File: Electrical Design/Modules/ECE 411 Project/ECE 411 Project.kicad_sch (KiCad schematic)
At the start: 31 parts, among them J1 5mm 9V Barrel, J2 BOOST, J3 Pheonix Connector, SW1 SW_Push, SW2 SW_Push, SW3 SW_Push, SW4 SW_Push, SW5 SW_Push, SW6 SW_Push, SW7 SW_Push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

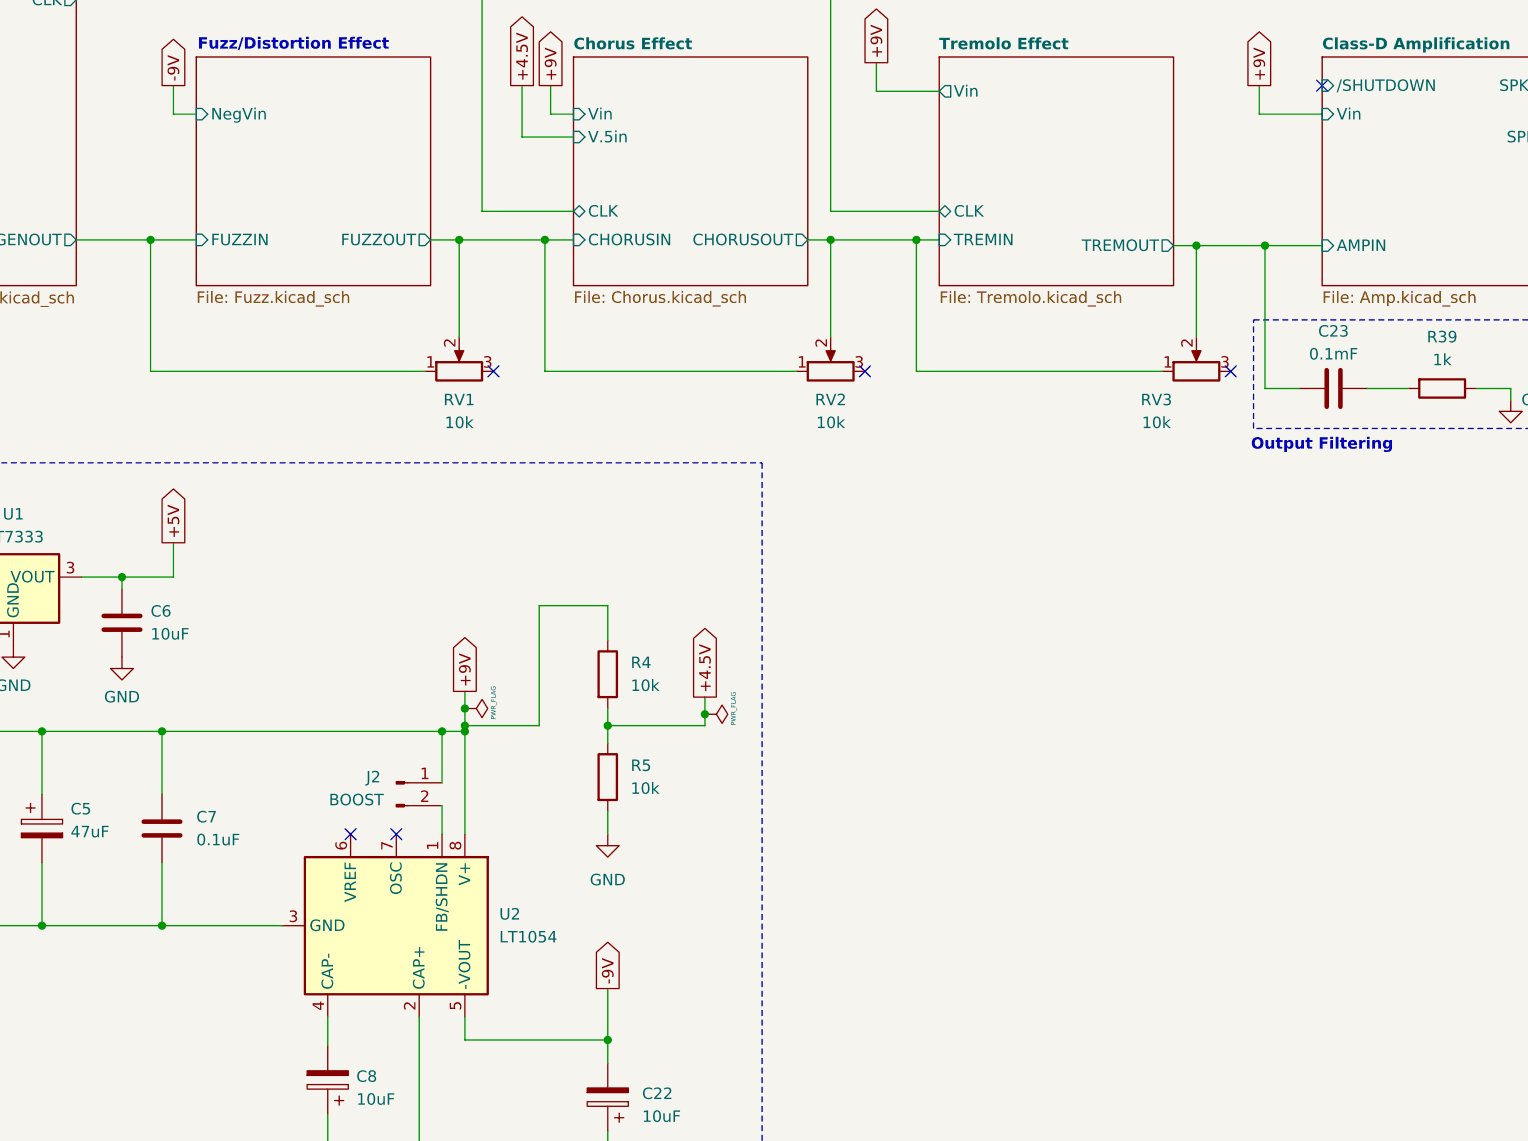
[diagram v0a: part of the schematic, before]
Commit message: bom changes
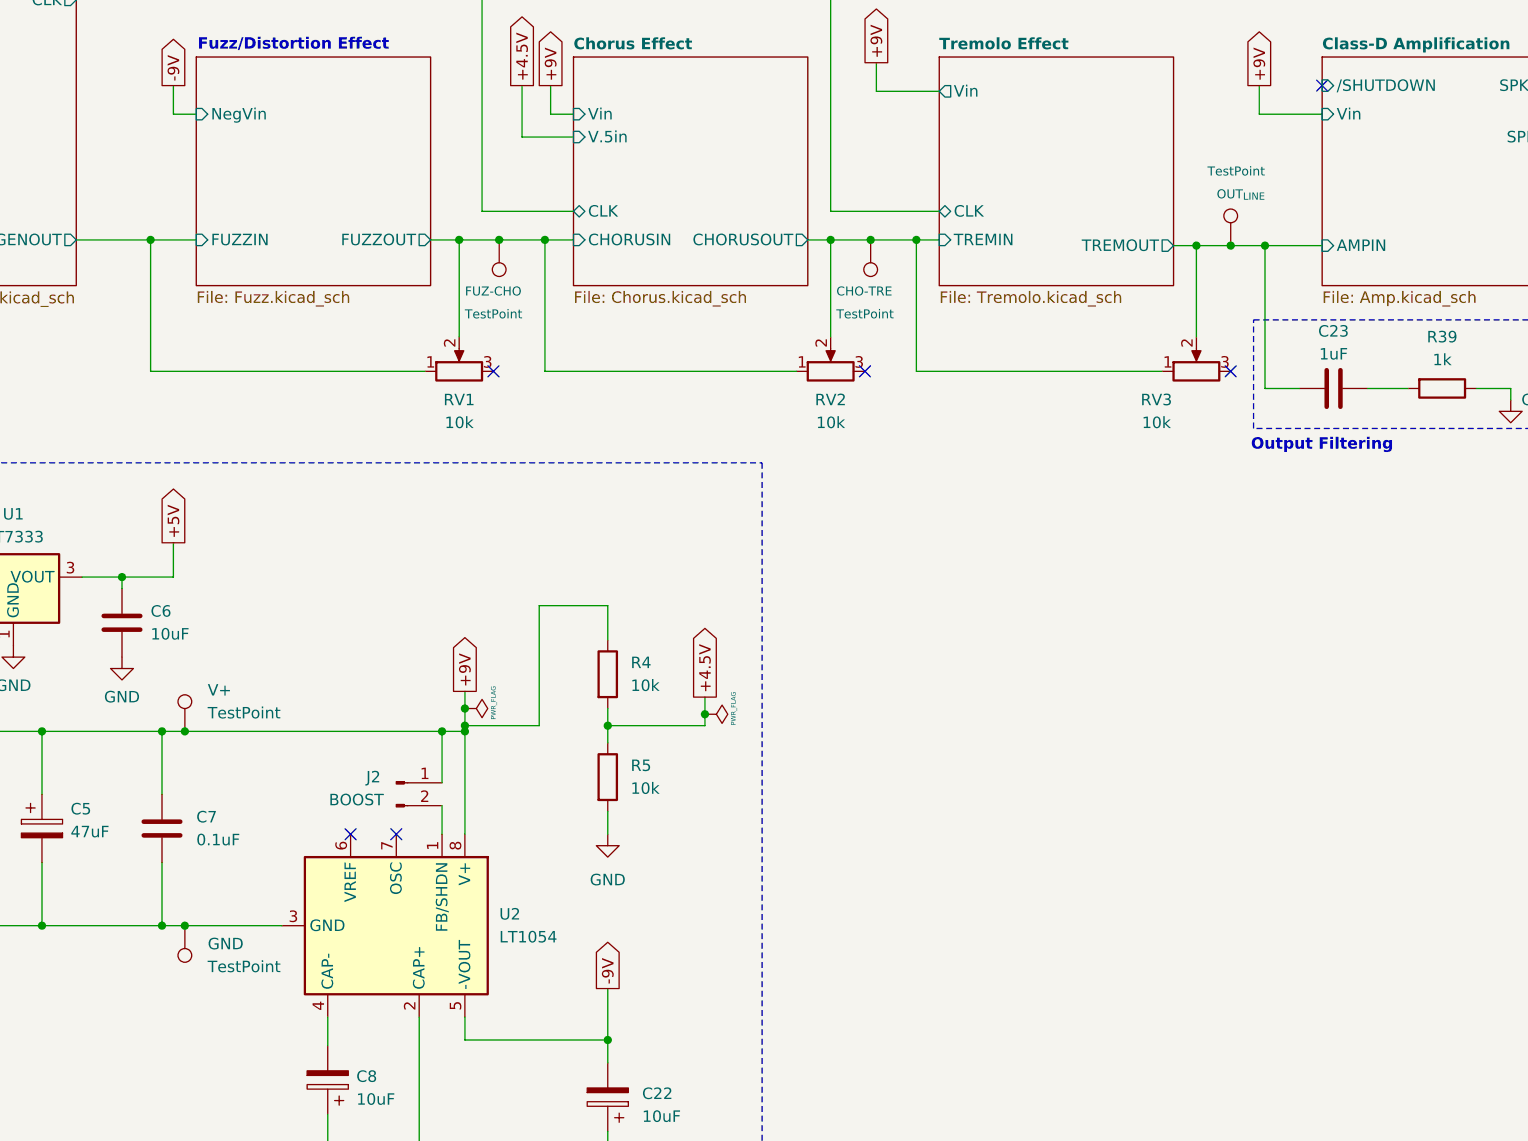
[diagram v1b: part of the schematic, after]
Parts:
- added CHO-TRE, FUZ-CHO, GND, OUT_{LINE}, V+: TestPoint, symbol Connector:TestPoint
- C22: On Hand (On Way) (none) -> (50); Part Number (none) -> UVR2C100MPD
- C23: value 0.1mF -> 1uF
- C43: On Hand (On Way) (none) -> (100); Part Number (none) -> CL21B104KBCNNNC
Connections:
- net +9V: now also V+.1
- net Chorus Effect/CHORUSIN: now also FUZ-CHO.1
- net Chorus Effect/CHORUSOUT: now also CHO-TRE.1
- net Class-D Amplification/AMPIN: now also OUT_{LINE}.1
- net GND: now also GND.1

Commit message: update kicad
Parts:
- OLED1: value ~ -> OLED-I2C
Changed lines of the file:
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@@
 			)
 		)
-		(property "Value" "~"
+		(property "Value" "OLED-I2C"
 			(at 94.615 45.72 0)
 			(effects

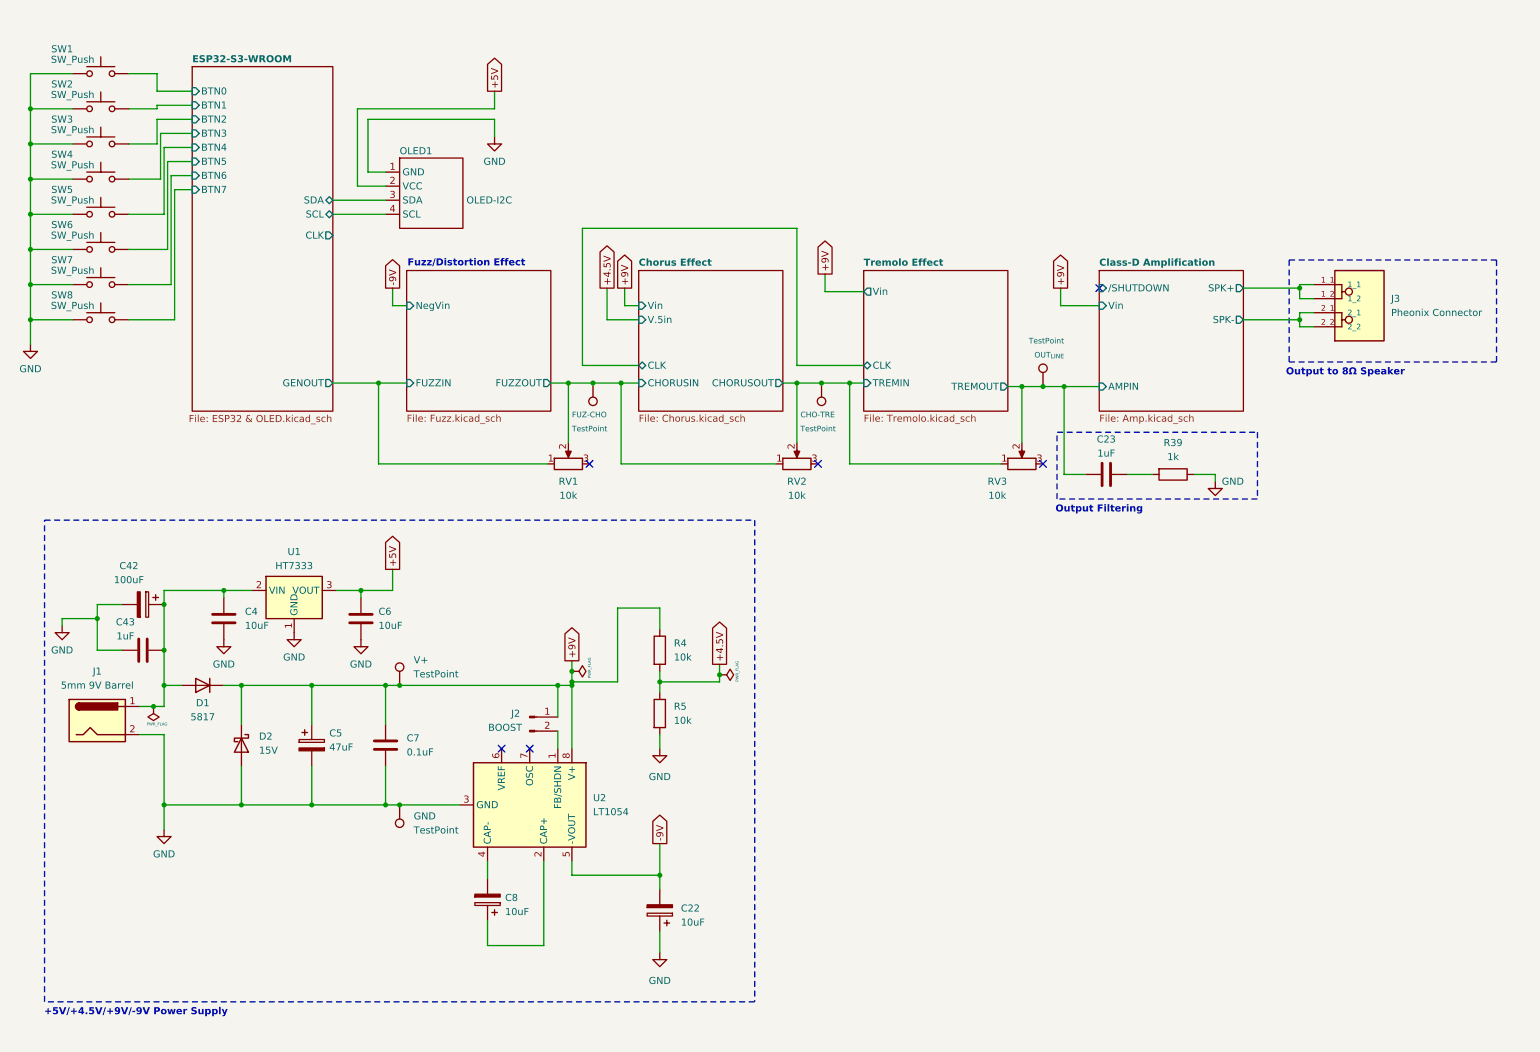
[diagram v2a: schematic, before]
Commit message: add switch to schematic
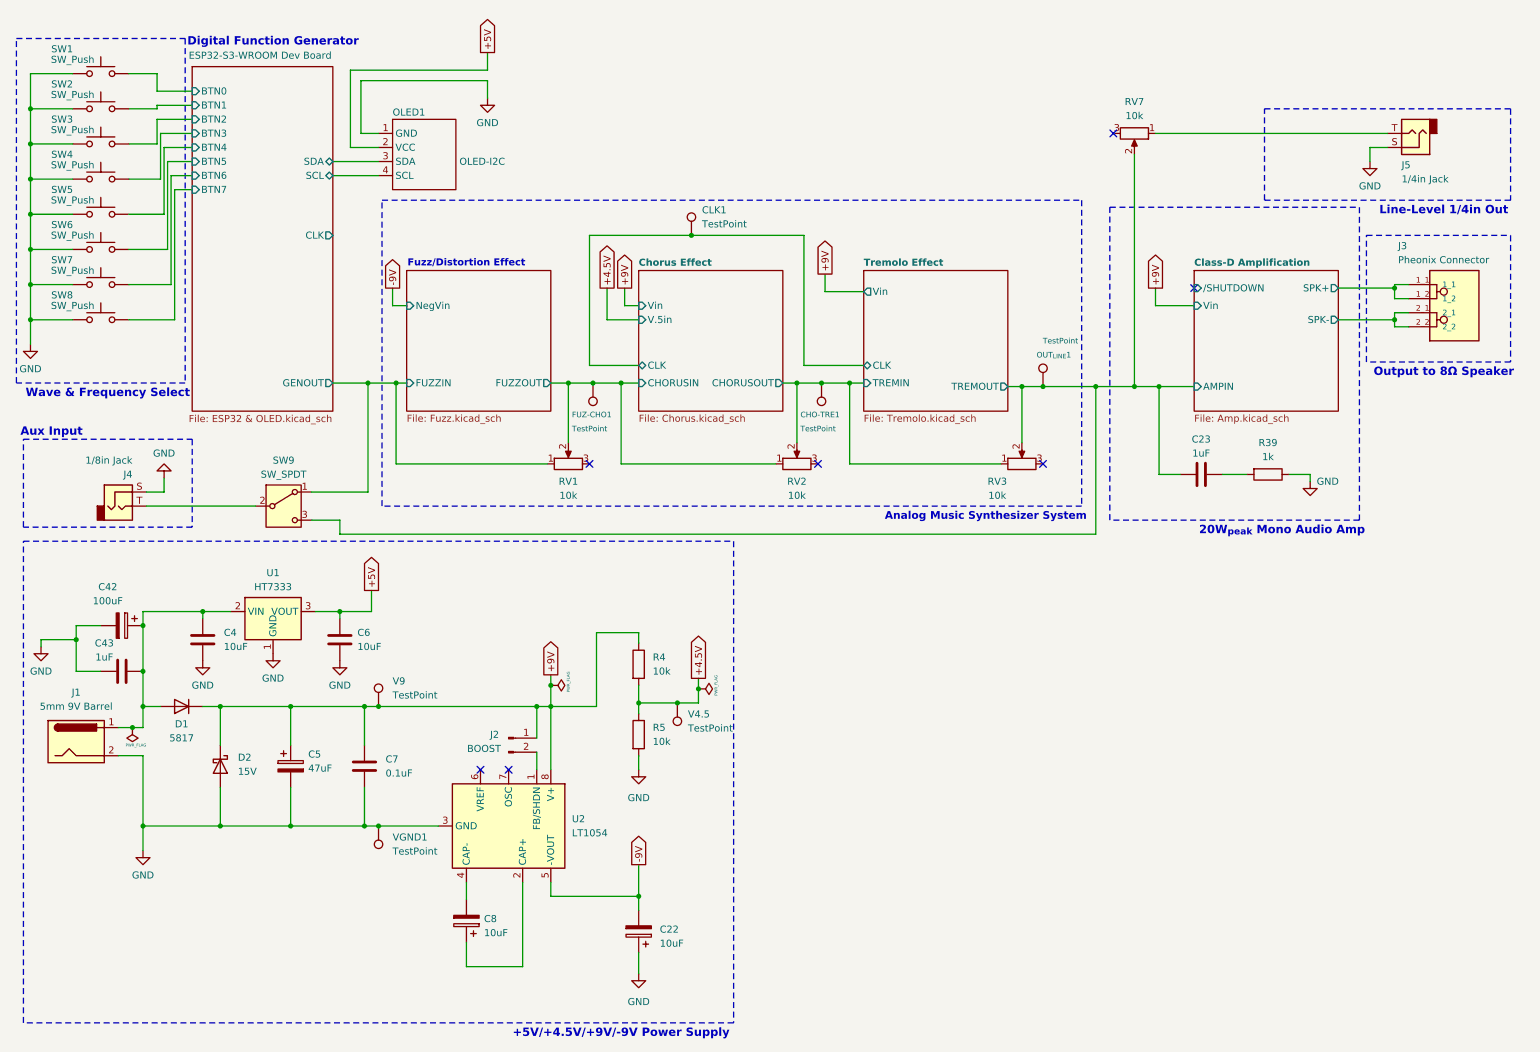
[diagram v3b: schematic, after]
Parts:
- added CLK1, V4.5: TestPoint, TestPoint:TestPoint_THTPad_2.5x2.5mm_Drill1.2mm, symbol Connector:TestPoint
- added J4: 1/8in Jack, symbol Connector_Audio:AudioJack2
- added J5: 1/4in Jack, symbol Connector_Audio:AudioJack2
- added RV7: 10k, Connector_PinSocket_2.54mm:PinSocket_1x03_P2.54mm_Vertical, symbol Device:R_Potentiometer
- added SW9: SW_SPDT, Button_Switch_THT:SW_Slide_SPDT_Angled_CK_OS102011MA1Q, symbol Switch:SW_SPDT
- CHO-TRE1: renamed from CHO-TRE; footprint (none) -> TestPoint:TestPoint_THTPad_2.5x2.5mm_Drill1.2mm
- FUZ-CHO1: renamed from FUZ-CHO; footprint (none) -> TestPoint:TestPoint_THTPad_2.5x2.5mm_Drill1.2mm
- OUT_{LINE}1: renamed from OUT_{LINE}; footprint (none) -> TestPoint:TestPoint_THTPad_2.5x2.5mm_Drill1.2mm
- V9: renamed from V+; footprint (none) -> TestPoint:TestPoint_THTPad_2.5x2.5mm_Drill1.2mm
- VGND1: renamed from GND; footprint (none) -> TestPoint:TestPoint_THTPad_2.5x2.5mm_Drill1.2mm
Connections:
- net +4.5V: now also V4.5.1
- net Chorus Effect/CLK: now also CLK1.1
- net Class-D Amplification/AMPIN: now also RV7.2, SW9.3 (C)
- net ESP32-S3-WROOM Dev Board/GENOUT: now also SW9.1 (A)
- net GND: now also J4.S, J5.S
- new net: J4.T, SW9.2 (B)
- new net: J5.T, RV7.1
- no-connect marks 6 -> 7
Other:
- sheet ESP32-S3-WROOM renamed ESP32-S3-WROOM Dev Board
- note added: "20W_{peak} Mono Audio Amp"
- note added: "Analog Music Synthesizer System"
- note added: "Aux Input"
- note added: "Digital Function Generator"
- note added: "Line-Level 1/4in Out"
- note added: "Wave & Frequency Select"
- note removed: "Output Filtering"
- moved on the sheet: C22, C23, C4, C42, C43, C5, C6, C7, C8, D1, D2, J1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

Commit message: PCB V2!!!
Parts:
- C42: footprint Capacitor_THT:CP_Radial_D6.3mm_P2.50mm -> Capacitor_THT:CP_Radial_D8.0mm_P3.50mm
- J2: footprint Connector_PinHeader_2.54mm:PinHeader_1x02_P2.54mm_Horizontal -> Connector_PinHeader_2.54mm:PinHeader_1x02_P2.54mm_Vertical
- J4: footprint (none) -> Connector_Audio:Jack_3.5mm_CUI_SJ-3523-SMT_Horizontal
- J5: footprint (none) -> Connector_PinSocket_2.54mm:PinSocket_1x02_P2.54mm_Vertical
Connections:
- net Class-D Amplification/SPK+: now also J3.2_1, J3.2_2; no longer J3.1_1, J3.1_2
- net Class-D Amplification/SPK-: now also J3.1_1, J3.1_2; no longer J3.2_1, J3.2_2
- net LineIn: now reaches J4.T, SW9.2 (B)
- net Vin: now reaches C4.1, C42.1, C43.2, D1.2 (A), J1.1, U1.2 (VIN)
- net LineOut: now reaches J5.T, RV7.1
- net LineOut: now also C23.1
- net Class-D Amplification/AMPIN renamed Tremolo Effect/TREMOUT
- net Tremolo Effect/TREMOUT: no longer C23.1
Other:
- moved on the sheet: J5, OUT_{LINE}1, RV3, RV7

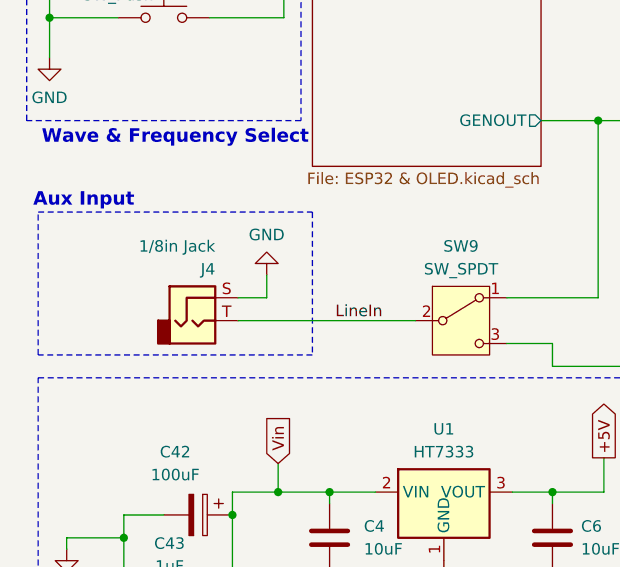
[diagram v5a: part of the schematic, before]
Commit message: oled test & schematic update
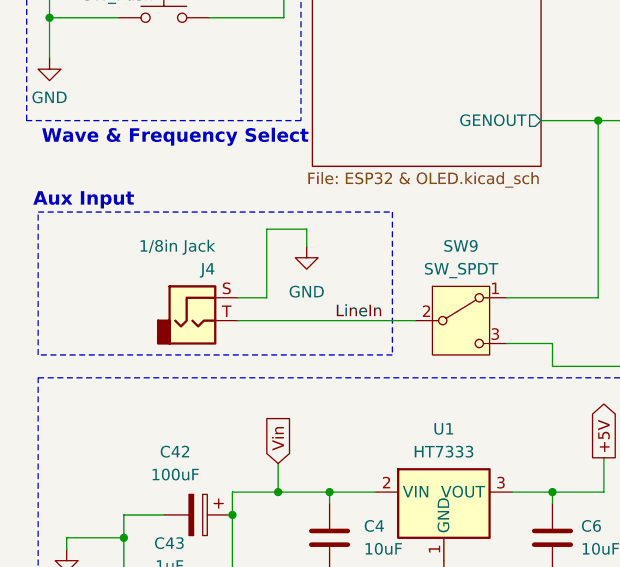
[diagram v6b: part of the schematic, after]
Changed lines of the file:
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@@
 	(wire
 		(pts
+			(xy 40.005 90.805) (xy 44.45 90.805)
+		)
+		(stroke
+			(width 0)
+			(type default)
+		)
+	)
+	(wire
+		(pts
 			(xy 70.485 38.735) (xy 78.74 38.735)
 		)
@@
 	(wire
 		(pts
+			(xy 40.005 90.805) (xy 40.005 98.425)
+		)
+		(stroke
+			(width 0)
+			(type default)
+		)
+	)
+	(wire
+		(pts
 			(xy 33.655 54.61) (xy 40.64 54.61)
 		)
@@
 	(wire
 		(pts
+			(xy 44.45 90.805) (xy 44.45 92.71)
+		)
+		(stroke
+			(width 0)
+			(type default)
+		)
+	)
+	(wire
+		(pts
 			(xy 98.425 22.225) (xy 73.66 22.225)
 		)
@@
 	(wire
 		(pts
-			(xy 40.005 95.885) (xy 40.005 98.425)
-		)
-		(stroke
-			(width 0)
-			(type default)
-		)
-	)
-	(wire
-		(pts
 			(xy 109.855 171.45) (xy 125.73 171.45)
 		)
@@
 	(rectangle
 		(start 14.605 88.9)
-		(end 45.085 104.775)
+		(end 53.975 104.775)
 		(stroke
 			(width 0)
@@
 	)
 	(symbol
-		(lib_id "power:GND")
-		(at 40.005 95.885 180)
-		(unit 1)
-		(exclude_from_sim no)
-		(in_bom yes)
-		(on_board yes)
-		(dnp no)
-		(fields_autoplaced yes)
-		(property "Reference" "#PWR029"
-			(at 40.005 89.535 0)
-			(effects
-				(font
-					(size 1.27 1.27)
-				)
-				(hide yes)
-			)
-		)
-		(property "Value" "GND"
-			(at 40.005 91.44 0)
-			(effects
-				(font
-					(size 1.27 1.27)
-				)
-			)
-		)
-		(property "Footprint" ""
-			(at 40.005 95.885 0)
-			(effects
-				(font
-					(size 1.27 1.27)
-				)
-				(hide yes)
-			)
-		)
-		(property "Datasheet" ""
-			(at 40.005 95.885 0)
-			(effects
-				(font
-					(size 1.27 1.27)
-				)
-				(hide yes)
-			)
-		)
-		(property "Description" "Power symbol creates a global label with name \"GND\" , ground"
-			(at 40.005 95.885 0)
-			(effects
-				(font
-					(size 1.27 1.27)
-				)
-				(hide yes)
-			)
-		)
-		(pin "1"
-		)
-		(instances
-			(project "ECE 411 Project"
-				(path "/2625e5a1-d0c8-41ce-941d-75d035a5f1c5"
-					(reference "#PWR029")
-					(unit 1)
-				)
-			)
-		)
-	)
-	(symbol
 		(lib_id "Device:D")
 		(at 43.18 137.16 180)
@@
 					(unit 1)
 				)
+			)
+		)
+	)
+	(symbol
+		(lib_id "power:GND")
+		(at 44.45 92.71 0)
+		(unit 1)
+		(exclude_from_sim no)
+		(in_bom yes)
+		(on_board yes)
+		(dnp no)
+		(fields_autoplaced yes)
+		(property "Reference" "#PWR026"
+			(at 44.45 99.06 0)
+			(effects
+				(font
+					(size 1.27 1.27)
+				)
+				(hide yes)
+			)
+		)
+		(property "Value" "GND"
+			(at 44.45 97.79 0)
+			(effects
+				(font
+					(size 1.27 1.27)
+				)
+			)
+		)
+		(property "Footprint" ""
+			(at 44.45 92.71 0)
+			(effects
+				(font
+					(size 1.27 1.27)
+				)
+				(hide yes)
+			)
+		)
+		(property "Datasheet" ""
+			(at 44.45 92.71 0)
+			(effects
+				(font
+					(size 1.27 1.27)
+				)
+				(hide yes)
+			)
+		)
+		(property "Description" "Power symbol creates a global label with name \"GND\" , ground"
+			(at 44.45 92.71 0)
+			(effects
+				(font
+					(size 1.27 1.27)
+				)
+				(hide yes)
+			)
+		)
+		(pin "1"
+		)
+		(instances
+			(project ""
+				(path "/2625e5a1-d0c8-41ce-941d-75d035a5f1c5"
+					(reference "#PWR026")
+					(unit 1)
+				)
